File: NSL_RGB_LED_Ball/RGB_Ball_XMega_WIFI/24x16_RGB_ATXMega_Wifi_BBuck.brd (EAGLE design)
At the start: 46.4 x 123.7 mm, 107 parts, among them IC2 TLC5947XLP, IC3 TLC5947XLP, IC4 TLC5947XLP, IC5 MCP73123, IC6 CC3000, IC7 MMA7455L, IC8 OPA344, X1 NX3225GA-16.000M-STD-CRG-2

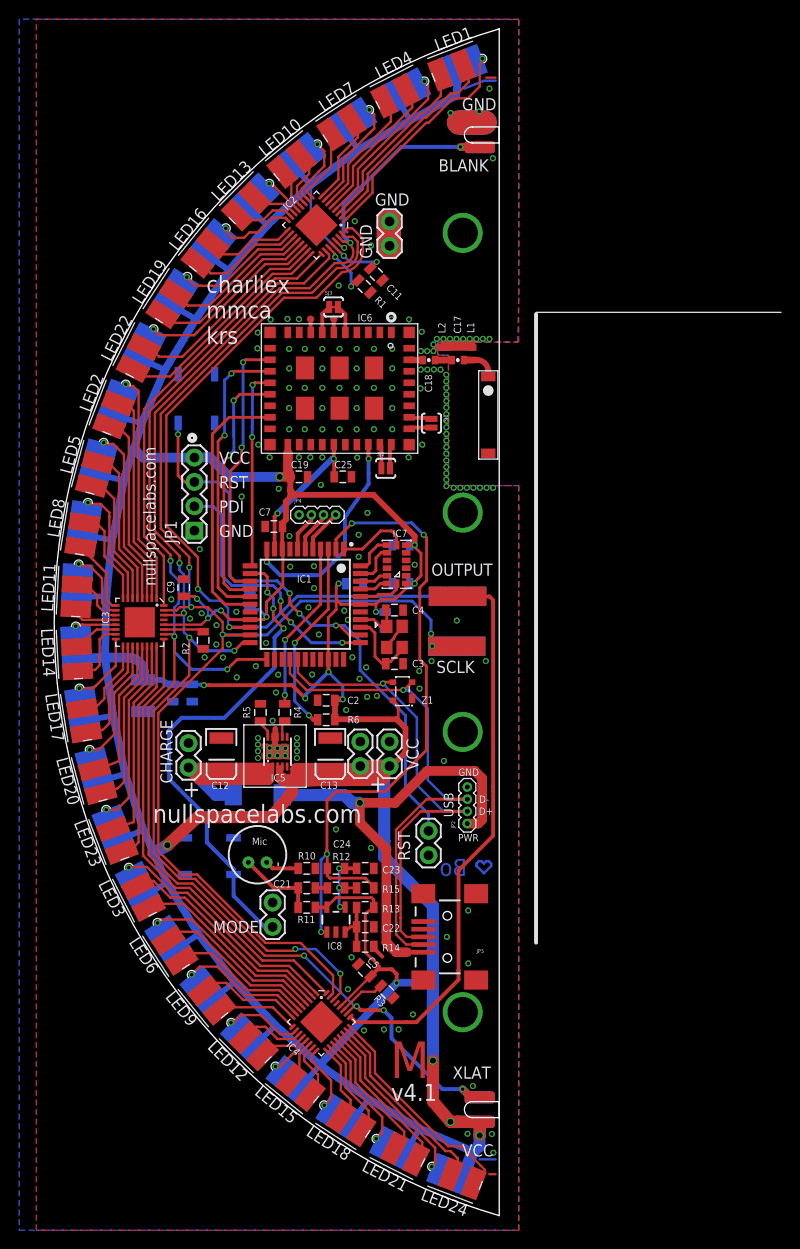
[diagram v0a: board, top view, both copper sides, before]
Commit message: 
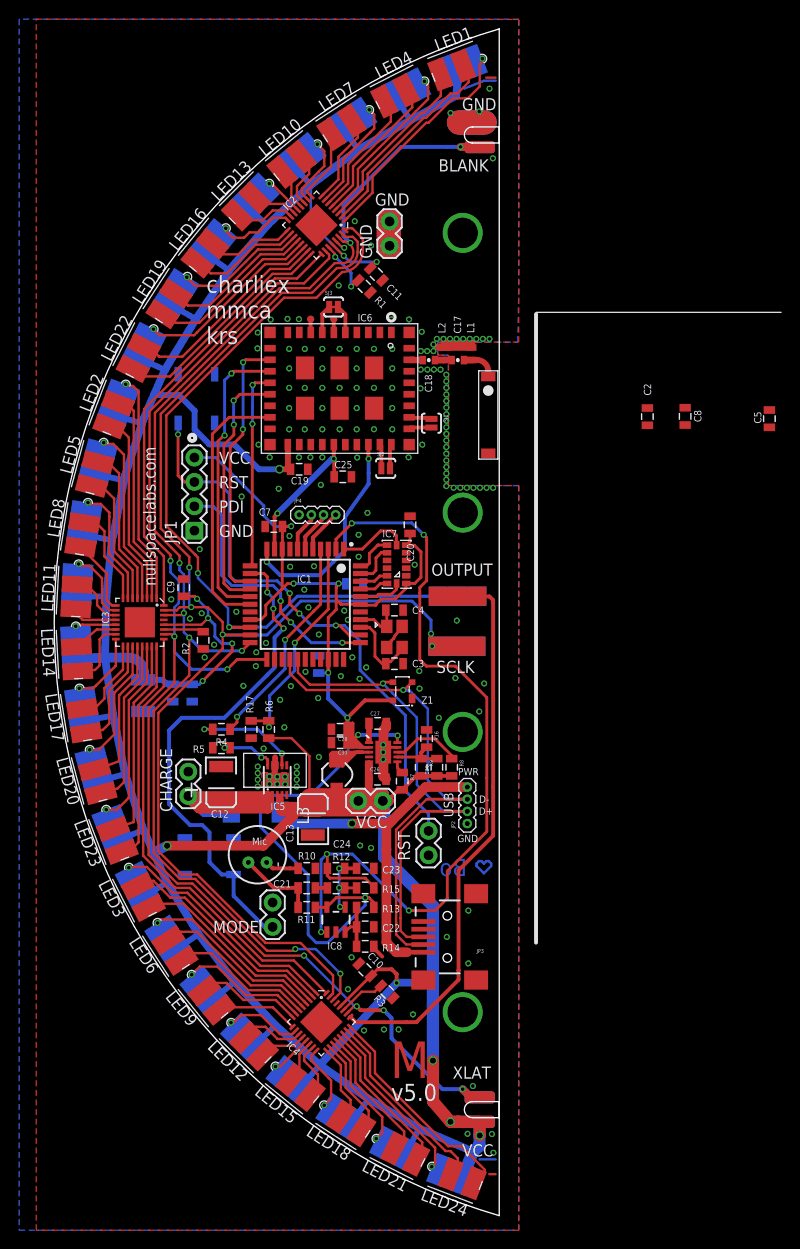
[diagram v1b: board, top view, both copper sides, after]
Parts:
- removed BATTERY1: (no value), SparkFun:1X02
- added C26, C28, C30: 10uF, CH_passive:0805
- added C27, C29: 0.1, CH_passive:0805
- added L3: 2.2uH 1.6A, CH_passive:1_3X1_3
- added R16, R9: see notes, CH_passive:0805
- added R17: 100K, slice_noshift:0805
- added R7, R8: 1M, CH_passive:0805
- added U1: TPS6120x, CH_TI:QFN_10_PAD
- R6: value 220K -> 100K
- moved C5 71.3 mm to (10.4, 21.2), turned to 270 degrees
- moved C2 44.7 mm to (-2.34, 21.4), turned to 270 degrees
- moved C10 40.3 mm to (-31.8, -36.2), flipped to the top, turned to 135 degrees
- moved C8 37.8 mm to (1.60, 21.5), flipped to the top
- moved C1 12.0 mm to (-36.6, -4.39), turned to 90 degrees
- moved C13 7.05 mm to (-37.2, -20.5), turned to 90 degrees
- moved R4 6.83 mm to (-46.7, -11.2), turned to 180 degrees
- moved VCC 6.18 mm to (-32.5, -18.6), turned to 0 degrees
- moved R6 6.08 mm to (-41.8, -11.2), turned to 90 degrees
- moved R5 5.48 mm to (-46.7, -13.1), turned to 0 degrees
- moved C12 2.97 mm to (-46.8, -16.7)
- moved CHARGE 2.97 mm to (-50.2, -15.6)
- moved IC5 2.97 mm to (-40.9, -16.5)
- moved C20 2.29 mm to (-27.1, 10.2), flipped to the top, turned to 270 degrees
- moved D1 1.81 mm to (-43.2, -19.8)
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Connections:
- new net +3V3: C1.1, C2.1, C20.2, C28.1, C30.1, C5.1, C6.1, C7.1, C8.1, IC1.19, IC1.31, IC1.39, IC1.9, IC7.1, IC7.6, IC8.5, JP1.4, R11.2, R13.2, U1.10, U1.2, Z1.4
- new net EN: R7.1, U1.6
- new net N$24: L3.P$2, U1.3
- new net N$30: C27.1, U1.1
- new net PS: R8.1, U1.8
- new net UVLO: C29.2, R16.2, R9.1, U1.7
- net BATTSENSE: now also R17.2
- net GND: now also C26.2, C27.2, C28.2, C30.2, JP2.1, R16.1, R17.1, U1.4, U1.9, U1.PAD@1, U1.PAD@2, U1.PAD@3, U1.PAD@4, U1.PAD@5; no longer BATTERY1.1, JP2.4, VCC.1
- net N$7: now also JP2.4; no longer JP2.1
- net VCC: now also C26.1, C29.1, L3.P$1, R7.2, R8.2, R9.2, U1.5, VCC.1; no longer BATTERY1.2, C1.1, C2.1, C20.2, C5.1, C6.1, C7.1, C8.1, IC1.19, IC1.31, IC1.39, IC1.9, IC7.1, IC7.6, IC8.5, JP1.4, R11.2, R13.2, Z1.4
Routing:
- net +3V3: track 0.00 -> 140.8 mm, vias 0 -> 8
- net VCC: track 557.5 -> 453.5 mm, vias 20 -> 12
- net MIC: track 69.8 -> 88.3 mm, vias 4 -> 5
- net N$24: track 0.00 -> 16.9 mm
- net N$7: track 48.9 -> 38.8 mm
- net GND: track 29.4 -> 38.7 mm, vias 170 -> 173
- net N$1: track 2.09 -> 11.3 mm, vias 0 -> 2
- net PS: track 0.00 -> 7.49 mm
- net UVLO: track 0.00 -> 6.36 mm
- net STAT: track 17.7 -> 22.7 mm
- net N$6: track 1.96 -> 6.17 mm, vias 0 -> 2
- net BATTSENSE: track 20.5 -> 23.6 mm
- net N$30: track 0.00 -> 2.76 mm
- net BUTTON: track 51.8 -> 53.2 mm
- net EN: track 0.00 -> 1.33 mm
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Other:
- board text added: "v5.0"
- board text removed: "v4.1"

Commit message: 
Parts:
- moved C2 46.0 mm to (-43.7, 1.37), flipped to the bottom, turned to 90 degrees
- moved C5 44.3 mm to (-23.9, -6.87), turned to 0 degrees
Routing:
- net +3V3: track 140.8 -> 162.3 mm, vias 8 -> 9
- net GND: vias 173 -> 177
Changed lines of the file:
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@@
 <attribute name="MPN" value="08055C105MAT2A" x="-36.6014" y="-4.3942" size="1.778" layer="28" rot="MR90" display="off"/>
 </element>
-<element name="C2" library="slice_noshift" package="0805" value=".1uF" x="-2.3368" y="21.4376" smashed="yes" rot="R270">
-<attribute name="NAME" x="-2.7051" y="24.892" size="0.762" layer="21" font="vector" ratio="12" rot="R270"/>
-<attribute name="VALUE" x="-3.7338" y="22.4536" size="0.4064" layer="27" rot="R270"/>
-<attribute name="VALUE" x="-3.7338" y="22.4536" size="0.4064" layer="27" rot="R270"/>
-<attribute name="OC_NEWARK" value="73T5385" x="-2.3368" y="21.4376" size="1.778" layer="27" rot="R270" display="off"/>
-<attribute name="MF" value="" x="-2.3368" y="21.4376" size="1.778" layer="27" rot="R270" display="off"/>
-<attribute name="MPN" value="08055C105MAT2A" x="-2.3368" y="21.4376" size="1.778" layer="27" rot="R270" display="off"/>
+<element name="C2" library="slice_noshift" package="0805" value=".1uF" x="-43.7388" y="1.3716" smashed="yes" rot="MR90">
+<attribute name="NAME" x="-44.1071" y="-2.0828" size="0.762" layer="22" font="vector" ratio="12" rot="MR90"/>
+<attribute name="VALUE" x="-45.1358" y="0.3556" size="0.4064" layer="28" rot="MR90"/>
+<attribute name="VALUE" x="-45.1358" y="0.3556" size="0.4064" layer="28" rot="MR90"/>
+<attribute name="OC_NEWARK" value="73T5385" x="-43.7388" y="1.3716" size="1.778" layer="28" rot="MR90" display="off"/>
+<attribute name="MF" value="" x="-43.7388" y="1.3716" size="1.778" layer="28" rot="MR90" display="off"/>
+<attribute name="MPN" value="08055C105MAT2A" x="-43.7388" y="1.3716" size="1.778" layer="28" rot="MR90" display="off"/>
 </element>
 <element name="VCC" library="SparkFun" package="1X02" value="" x="-32.4612" y="-18.6182" smashed="yes">
@@
 <attribute name="MPN" value="" x="-49.3522" y="23.3172" size="1.778" layer="28" rot="MR90" display="off"/>
 </element>
-<element name="C5" library="slice_noshift" package="0805" value=".1uF" x="10.379253125" y="21.224421875" smashed="yes" rot="R270">
-<attribute name="NAME" x="8.780059375" y="21.9684375" size="0.762" layer="21" font="vector" ratio="12" rot="R270"/>
-<attribute name="VALUE" x="8.982153125" y="22.240390625" size="0.4064" layer="27" rot="R270"/>
-<attribute name="VALUE" x="8.982153125" y="22.240390625" size="0.4064" layer="27" rot="R270"/>
-<attribute name="OC_NEWARK" value="73T5385" x="10.379253125" y="21.224421875" size="1.778" layer="27" rot="R270" display="off"/>
-<attribute name="MF" value="" x="10.379253125" y="21.224421875" size="1.778" layer="27" rot="R270" display="off"/>
-<attribute name="MPN" value="08055C105MAT2A" x="10.379253125" y="21.224421875" size="1.778" layer="27" rot="R270" display="off"/>
+<element name="C5" library="slice_noshift" package="0805" value=".1uF" x="-23.891421875" y="-6.867346875" smashed="yes">
+<attribute name="NAME" x="-22.0954375" y="-7.171140625" size="0.762" layer="21" font="vector" ratio="12"/>
+<attribute name="VALUE" x="-24.907390625" y="-8.264446875" size="0.4064" layer="27"/>
+<attribute name="VALUE" x="-24.907390625" y="-8.264446875" size="0.4064" layer="27"/>
+<attribute name="OC_NEWARK" value="73T5385" x="-23.891421875" y="-6.867346875" size="1.778" layer="27" display="off"/>
+<attribute name="MF" value="" x="-23.891421875" y="-6.867346875" size="1.778" layer="27" display="off"/>
+<attribute name="MPN" value="08055C105MAT2A" x="-23.891421875" y="-6.867346875" size="1.778" layer="27" display="off"/>
 </element>
 <element name="MODE" library="24x16_RGB" package="1X02" value="" x="-41.402" y="-29.21" smashed="yes" rot="R270">
@@
 <wire x1="-35.7124" y1="-26.3906" x2="-35.7124" y2="-25.6684" width="0.3048" layer="1"/>
 <wire x1="-35.7124" y1="-25.6684" x2="-35.698" y2="-25.654" width="0.3048" layer="1"/>
-<wire x1="-25.3492" y1="4.3434" x2="-26.0604" y2="3.6322" width="0.3048" layer="1"/>
-<wire x1="-26.0604" y1="3.6322" x2="-26.0604" y2="3.0734" width="0.3048" layer="1"/>
-<wire x1="-26.0604" y1="-3.8862" x2="-26.0604" y2="3.0734" width="0.3048" layer="1"/>
-<wire x1="-26.0604" y1="-3.8862" x2="-25.3746" y2="-4.572" width="0.3048" layer="1"/>
+<wire x1="-25.6032" y1="2.54" x2="-25.6032" y2="3.0734" width="0.3048" layer="1"/>
 <wire x1="-35.7378" y1="-24.1554" x2="-33.0962" y2="-24.1554" width="0.3048" layer="16"/>
 <wire x1="-33.0962" y1="-24.1554" x2="-27.2034" y2="-30.0482" width="0.3048" layer="16"/>
@@
 <wire x1="-19.0754" y1="-16.2306" x2="-19.0754" y2="-7.8486" width="0.3048" layer="1"/>
 <wire x1="-19.0754" y1="-7.8486" x2="-22.352" y2="-4.572" width="0.3048" layer="1"/>
-<wire x1="-22.352" y1="-4.572" x2="-25.3746" y2="-4.572" width="0.3048" layer="1"/>
 <wire x1="-19.2532" y1="-21.9964" x2="-19.0754" y2="-21.8186" width="0.3048" layer="1"/>
 <wire x1="-19.0754" y1="-21.8186" x2="-19.0754" y2="-16.2306" width="0.3048" layer="1"/>
+<wire x1="-25.3492" y1="4.3434" x2="-25.6032" y2="4.0894" width="0.3048" layer="1"/>
+<wire x1="-25.6032" y1="4.0894" x2="-25.6032" y2="2.54" width="0.3048" layer="1"/>
+<wire x1="-25.6032" y1="2.54" x2="-25.6032" y2="-3.8608" width="0.3048" layer="1"/>
+<wire x1="-25.6032" y1="-3.8608" x2="-24.892" y2="-4.572" width="0.3048" layer="1"/>
+<wire x1="-24.892" y1="-4.572" x2="-22.352" y2="-4.572" width="0.3048" layer="1"/>
 </signal>
 <signal name="CHARGE">
@@
 <via x="-39.6494" y="8.9916" extent="1-16" drill="0.3556"/>
 <via x="-32.3342" y="-5.8928" extent="1-16" drill="0.3556"/>
-<via x="-22.352" y="-5.8166" extent="1-16" drill="0.3556"/>
+<via x="-22.1996" y="-5.7404" extent="1-16" drill="0.3556"/>
 <via x="-31.6484" y="-4.699" extent="1-16" drill="0.3556"/>
 <via x="-19.3548" y="-6.3754" extent="1-16" drill="0.3556"/>
@@
 <via x="-48.9966" y="7.62" extent="1-16" drill="0.3556"/>
 <via x="-40.1828" y="-10.9474" extent="1-16" drill="0.3556"/>
-<via x="-36.576" y="-14.0462" extent="1-16" drill="0.3556"/>
+<via x="-36.9316" y="-16.51" extent="1-16" drill="0.3556"/>
 <via x="-31.877" y="-42.545" extent="1-16" drill="0.3556"/>
 <via x="-28.2702" y="-42.4434" extent="1-16" drill="0.3556"/>
@@
 <via x="-24.0792" y="-9.9568" extent="1-16" drill="0.3556"/>
 <via x="-19.8628" y="-9.2964" extent="1-16" drill="0.3556"/>
-<via x="-26.1112" y="-5.08" extent="1-16" drill="0.3556"/>
+<via x="-27.8892" y="-5.6134" extent="1-16" drill="0.3556"/>
 <via x="-51.9684" y="2.3876" extent="1-16" drill="0.3556"/>
 <via x="-23.2918" y="16.1798" extent="1-16" drill="0.3556"/>
@@
 <via x="-29.8704" y="-14.3002" extent="1-16" drill="0.3556"/>
 <via x="-29.8704" y="-13.5382" extent="1-16" drill="0.3556"/>
-<wire x1="1.6002" y1="20.563" x2="10.379253125" y2="20.324421875" width="0" layer="19" extent="1-1"/>
-<wire x1="-2.3368" y1="20.5376" x2="1.6002" y2="20.563" width="0" layer="19" extent="1-1"/>
-<wire x1="-18.415" y1="14.0208" x2="-2.3368" y2="20.5376" width="0" layer="19" extent="1-1"/>
+<via x="-30.734" y="1.016" extent="1-16" drill="0.3556"/>
+<via x="-32.4612" y="-14.3764" extent="1-16" drill="0.3556"/>
+<via x="-32.3342" y="-16.764" extent="1-16" drill="0.3556"/>
+<via x="-34.5694" y="-16.1798" extent="1-16" drill="0.3556"/>
+<wire x1="-18.415" y1="14.0208" x2="1.6002" y2="20.563" width="0" layer="19" extent="1-1"/>
 </signal>
 <signal name="N$7">
@@
 <wire x1="-30.099" y1="2.413" x2="-28.6258" y2="2.413" width="0.3048" layer="1"/>
 <wire x1="-28.6258" y1="2.413" x2="-27.5082" y2="3.5306" width="0.3048" layer="1"/>
-<wire x1="-27.5082" y1="3.5306" x2="-27.5082" y2="4.0104" width="0.3048" layer="1"/>
+<wire x1="-27.5082" y1="3.5306" x2="-27.5082" y2="3.9878" width="0.3048" layer="1"/>
+<wire x1="-27.5082" y1="3.9878" x2="-27.5082" y2="4.0104" width="0.3048" layer="1"/>
 <wire x1="-27.5082" y1="4.0104" x2="-27.4734" y2="4.0452" width="0.3048" layer="1"/>
 <wire x1="-27.4734" y1="8.0452" x2="-27.4668" y2="8.0518" width="0.3048" layer="1"/>
@@
 <wire x1="-35.6108" y1="-5.2578" x2="-35.6472" y2="-5.2942" width="0.3048" layer="16"/>
 <wire x1="-35.6472" y1="-5.2942" x2="-36.6014" y2="-5.2942" width="0.3048" layer="16"/>
-<wire x1="1.6002" y1="22.363" x2="10.379253125" y2="22.124421875" width="0" layer="19" extent="1-1"/>
-<wire x1="-2.3368" y1="22.3376" x2="1.6002" y2="22.363" width="0" layer="19" extent="1-1"/>
-<wire x1="-25.9334" y1="7.3406" x2="-2.3368" y2="22.3376" width="0" layer="19" extent="1-1"/>
+<wire x1="-28.8798" y1="-8.1788" x2="-27.813" y2="-9.2456" width="0.3048" layer="1"/>
+<wire x1="-27.813" y1="-9.2456" x2="-25.7302" y2="-9.2456" width="0.3048" layer="1"/>
+<wire x1="-25.7302" y1="-9.2456" x2="-25.0444" y2="-8.5598" width="0.3048" layer="1"/>
+<wire x1="-25.0444" y1="-8.5598" x2="-25.0444" y2="-6.3246" width="0.3048" layer="1"/>
+<wire x1="-25.0444" y1="-6.3246" x2="-25.0444" y2="-5.8166" width="0.3048" layer="1"/>
+<wire x1="-25.0444" y1="-5.8166" x2="-26.289" y2="-4.572" width="0.3048" layer="1"/>
+<wire x1="-26.289" y1="-4.572" x2="-26.289" y2="2.3622" width="0.3048" layer="1"/>
+<wire x1="-26.289" y1="2.3622" x2="-27.5082" y2="3.5814" width="0.3048" layer="1"/>
+<wire x1="-27.5082" y1="3.5814" x2="-27.5082" y2="3.9878" width="0.3048" layer="1"/>
+<wire x1="-43.7484" y1="0.2796" x2="-44.907" y2="0.2796" width="0.3048" layer="1"/>
+<wire x1="-44.907" y1="0.2796" x2="-45.0342" y2="0.1524" width="0.3048" layer="1"/>
+<via x="-45.0342" y="0.1524" extent="1-16" drill="0.3556"/>
+<wire x1="-45.0342" y1="0.1524" x2="-44.715" y2="0.4716" width="0.3048" layer="16"/>
+<wire x1="-44.715" y1="0.4716" x2="-43.7388" y2="0.4716" width="0.3048" layer="16"/>
+<wire x1="-24.791421875" y1="-6.867346875" x2="-25.0444" y2="-6.61436875" width="0.3048" layer="1"/>
+<wire x1="-25.0444" y1="-6.61436875" x2="-25.0444" y2="-6.3246" width="0.3048" layer="1"/>
+<wire x1="-25.9334" y1="7.3406" x2="1.6002" y2="22.363" width="0" layer="19" extent="1-1"/>
 </signal>
 <signal name="N$24">
